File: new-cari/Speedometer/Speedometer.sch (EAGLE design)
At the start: 3 parts, among them X1 JST-XH-03-PIN-LONG-PAD

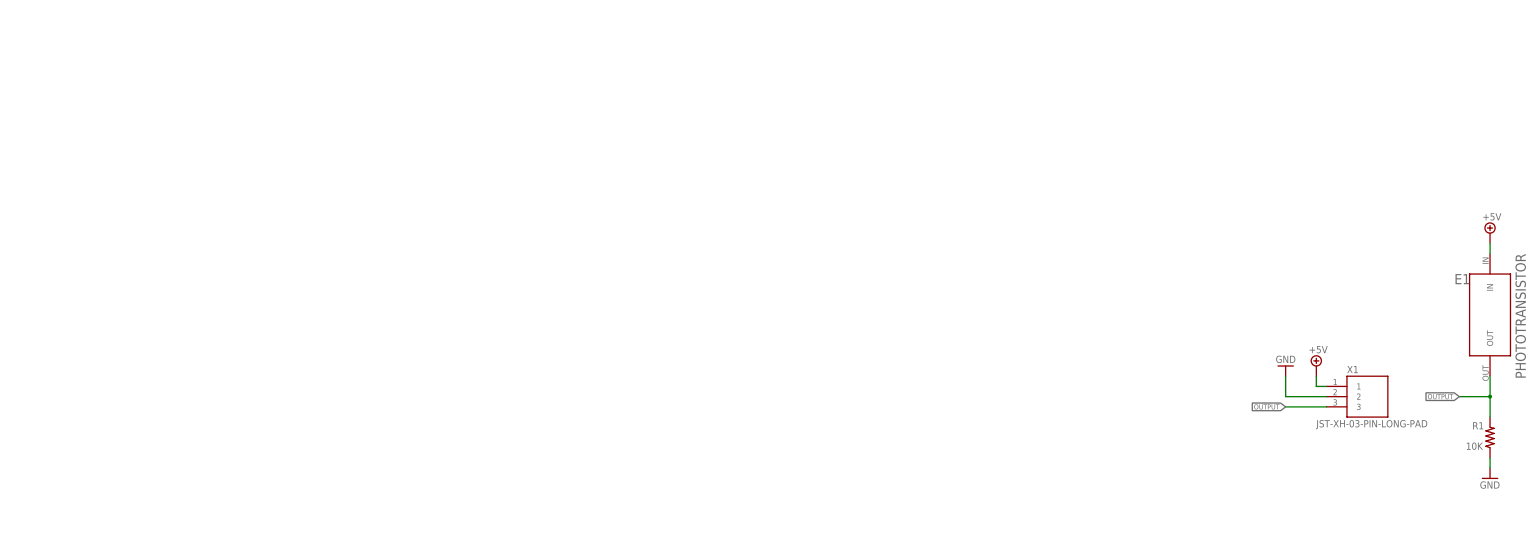
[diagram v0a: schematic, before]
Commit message: Created Speedometer board
Created board file and removed other unused files
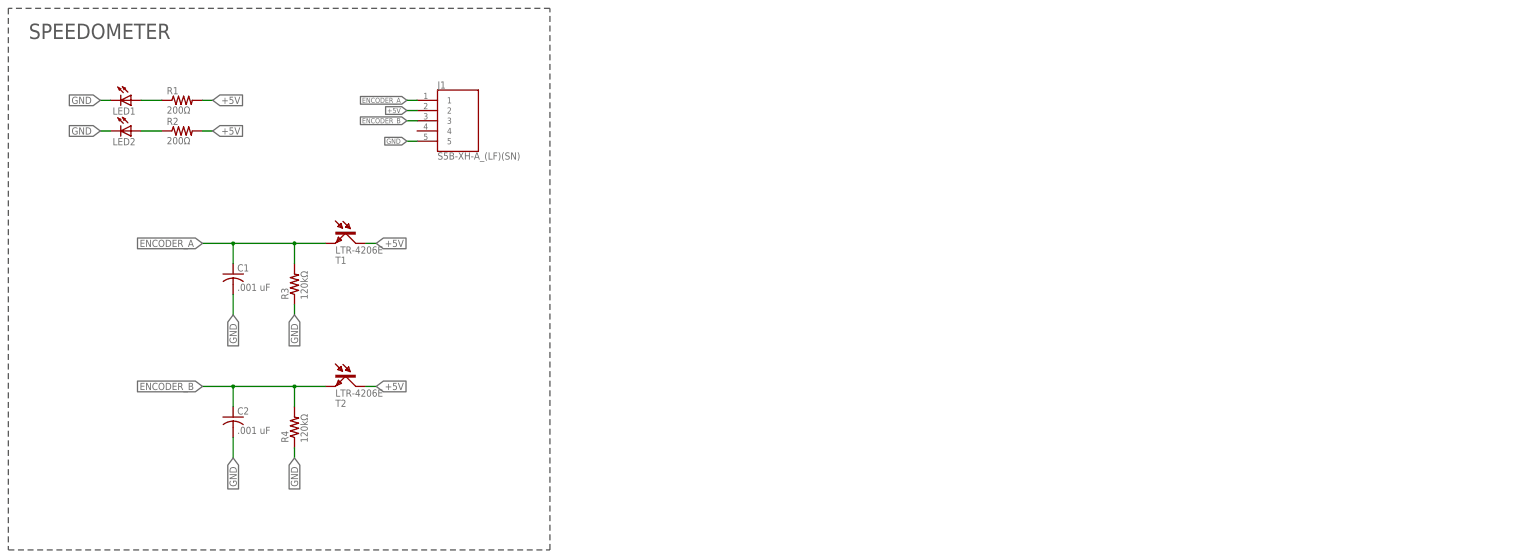
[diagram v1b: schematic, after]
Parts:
- removed E1: PHOTOTRANSISTOR, SpeedometerParts:PHOTOTRANSISTOR
- removed X1: JST-XH-03-PIN-LONG-PAD, RoboJackets-Connectors:JST-XH-03-PIN-LONG-PAD
- added C1, C2: .001 uF, rcl:C-USC0603
- added J1: S5B-XH-A_(LF)(SN), RoboJackets-Connectors:S5B-XH-A_(LF)(SN)
- added LED1, LED2: (no value), adafruit:LED3MM
- added R2: 200Ω, rcl:R-US_R0603
- added R3, R4: 120kΩ, rcl:R-US_R0603
- added T1, T2: LTR-4206E, LTR-4206E:LTR-4206E
- R1: value 10K -> 200Ω
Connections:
- removed net OUTPUT: E1.OUT, R1.2, X1.3
- new net ENCODER_A: C1.1, J1.1, R3.2, T1.E
- new net ENCODER_B: C2.1, J1.3, R4.2, T2.E
- new net N$1: LED1.A, R1.1
- new net N$2: LED2.A, R2.1
- net +5V: now also J1.2, R1.2, R2.2, T1.C, T2.C; no longer E1.IN, X1.1
- net GND: now also C1.2, C2.2, J1.5, LED1.C, LED2.C, R3.1, R4.1; no longer R1.1, X1.2
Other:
- note added: "SPEEDOMETER"
- moved on the sheet: R1
